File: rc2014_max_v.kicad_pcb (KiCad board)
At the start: 4 copper layers, 101.6 x 50.8 mm, 128 parts, among them J1 M3 Mounting Hole, J2 Conn_01x40, J3 Conn_01x24, J4 USB_B_Micro, J5 AVR-JTAG-10, J6 Pro Bus, J7 PMOD1, J8 PMOD, SW1 SW_Push, SW2 SW_Push, U1 TXB0108PWR, U10 FT2232H, U11 5M1270ZT144C5N, U12 93LCxxBxxOT, U13 IS61LV5128AL-10TLI, U14 Si5351A-B-GT, U15 TXB0108PWR, U16 TXB0108PWR, U18 MIC5356-SGYMME, U2 TXB0108PWR, U3 TXB0108PWR, U4 TXB0108PWR, U5 TXB0108PWR, U6 TXB0108PWR, U7 TXB0108PWR, U8 MIC5356-SGYMME, U9 TPD2EUSB30, X1 CB3LV-3I-100M0000, Y1 25MHZ 8PF

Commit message: Updated BOM
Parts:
- removed C20, C22: 100nF, Capacitor_SMD:C_0603_1608Metric_Pad1.05x0.95mm_HandSolder
- removed C21: 2.2uF, Capacitor_SMD:C_0603_1608Metric_Pad1.05x0.95mm_HandSolder
- removed U10: FT2232H, Package_QFP:LQFP-64_10x10mm_P0.5mm
- added JP2: Jumper_3_Bridged12, Connector_PinHeader_2.54mm:PinHeader_1x03_P2.54mm_Horizontal, F.Cu at (163.2, 80.8)
- JP1: footprint Connector_PinHeader_2.54mm:PinHeader_1x03_P2.54mm_Vertical -> Connector_PinHeader_2.54mm:PinHeader_1x03_P2.54mm_Horizontal
- RN8, RN9: moved to B.Cu
- U8: value MIC5356-SGYMME -> FT2232H; footprint Package_SO:MSOP-8-1EP_3x3mm_P0.65mm_EP2.5x3mm_Mask1.73x2.36mm_ThermalVias -> Package_QFP:TQFP-64_10x10mm_P0.5mm; moved to F.Cu
- moved U8 23.7 mm to (150.8, 103.3), turned to 180 degrees
- moved U16 8.59 mm to (117.6, 86.5)
- moved RN4 8.48 mm to (157.8, 110.9)
- moved C35 8.05 mm to (117.6, 83.5)
- moved D1 6.27 mm to (148.7, 111.6)
- moved R8 6.27 mm to (152.4, 111.6)
- moved R7 6.11 mm to (167.0, 83.8)
- moved C23 6.00 mm to (169.1, 85.7)
- moved RN8 5.86 mm to (164.0, 108.9)
- moved RN9 5.70 mm to (164.0, 116.3)
- moved JP1 2.65 mm to (84.0, 89.2)
- moved C34 2.55 mm to (105.0, 83.6)
- moved RN3 2.44 mm to (141.1, 79.7)
- moved J6 2.40 mm to (92.4, 80.6)
- moved U15 2.21 mm to (104.7, 86.7)
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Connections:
- C10 pad 1: +3V3 -> 3V3
- C11 pad 1: +3V3 -> 3V3
- C12 pad 1: +3V3 -> 3V3
- C13 pad 1: +3V3 -> 3V3
- C14 pad 1: +3V3 -> 3V3
- C15 pad 2: 5V -> 5V_R
- C24 pad 1: +3V3 -> 3V3
- C25 pad 1: +3V3 -> 3V3
- C26 pad 1: +3V3 -> 3V3
- C27 pad 1: +3V3 -> 3V3
- C28 pad 1: +1V8 -> 1V8
- C29 pad 1: +1V8 -> 1V8
- C30 pad 1: +1V8 -> 1V8
- C31 pad 1: +3V3 -> 3V3
- C32 pad 1: +3V3 -> 3V3
- C33 pad 1: +3V3 -> 3V3
- C38 pad 1: +3V3 -> GND
- C39 pad 1: +3V3 -> GND
- C40 pad 1: +3V3 -> GND
- C41 pad 1: +3V3 -> GND
- C8 pad 1: +3V3 -> 3V3
- C9 pad 1: +3V3 -> 3V3
- J2 pad 18: 5V -> 5V_R
- J3 pad 2: 5V -> 5V_R
- J4 pad 1: Net-(C21-Pad1) -> 5V_U
- J5 pad 4: +3V3 -> 3V3
- J5 pad 6: +3V3 -> 3V3
- J7 pad 12: +3V3 -> GND
- J7 pad 6: +3V3 -> GND
- J8 pad 12: +3V3 -> GND
- J8 pad 6: +3V3 -> GND
- JP1 pad 1: +3V3 -> 3V3
- L1 pad 1: +3V3 -> 3V3
- L2 pad 1: +3V3 -> 3V3
- R10 pad 1: +3V3 -> 3V3
- R11 pad 1: +3V3 -> 3V3
- R13 pad 1: +3V3 -> 3V3
- R14 pad 1: +3V3 -> 3V3
- R6 pad 1: +3V3 -> 3V3
- R8 pad 1: +3V3 -> 3V3
- RN1 pad 5: +3V3 -> 3V3
- RN1 pad 6: +3V3 -> 3V3
- RN1 pad 7: +3V3 -> 3V3
- RN1 pad 8: +3V3 -> 3V3
- RN3 pad 5: +3V3 -> 3V3
- RN3 pad 6: +3V3 -> 3V3
- RN3 pad 7: +3V3 -> 3V3
- RN4 pad 5: +3V3 -> 3V3
- RN4 pad 6: +3V3 -> 3V3
- RN4 pad 7: +3V3 -> 3V3
- RN4 pad 8: +3V3 -> 3V3
- RN5 pad 5: +3V3 -> GND
- RN5 pad 6: +3V3 -> GND
- RN5 pad 7: +3V3 -> GND
- RN5 pad 8: +3V3 -> GND
- RN6 pad 5: +3V3 -> 3V3
- RN6 pad 6: +3V3 -> 3V3
- RN6 pad 7: +3V3 -> 3V3
- RN6 pad 8: +3V3 -> 3V3
- RN7 pad 5: +3V3 -> 3V3
- RN7 pad 6: +3V3 -> 3V3
- RN7 pad 7: +3V3 -> 3V3
- RN7 pad 8: +3V3 -> 3V3
- U1 pad 2: +3V3 -> 3V3
- U12 pad 6: +3V3 -> 3V3
- U13 pad 11: +3V3 -> GND
- U13 pad 33: +3V3 -> GND
- U14 pad 1: +3V3 -> 3V3
- U14 pad 7: +3V3 -> 3V3
- U15 pad 2: +3V3 -> 3V3
- U16 pad 2: +3V3 -> 3V3
- U2 pad 2: +3V3 -> 3V3
- U3 pad 2: +3V3 -> 3V3
- U4 pad 2: +3V3 -> 3V3
- U5 pad 2: +3V3 -> 3V3
- U6 pad 2: +3V3 -> 3V3
- U7 pad 2: +3V3 -> 3V3
- U8 pad 1: Net-(C21-Pad1) -> GND
- U8 pad 2: GND -> CLK_12Mhz
- U8 pad 4: Net-(C21-Pad1) -> Net-(C18-Pad1)
- U8 pad 5: Net-(C21-Pad1) -> GND
- U8 pad 6: (no net) -> Net-(R5-Pad2)
- U8 pad 7: +1V8 -> Net-(J4-Pad3)
- U8 pad 8: +3V3 -> Net-(J4-Pad2)
- U8 pad 9: GND -> Net-(C16-Pad1)
- X1 pad 1: +3V3 -> 3V3
- X1 pad 4: +3V3 -> 3V3
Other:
- board text added: "PWR"
- board text removed: "JTAG PWR"

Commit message: updated descriptions and part #'s
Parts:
- D2, D3, D4, D5, D6, D7, D8, D9: value Blue -> Red
- RN10, RN11: moved to B.Cu
- U12: value 93LCxxBxxOT -> 93LC46BT-I/OT
- moved RN11 6.44 mm to (163.2, 98.9), turned to 0 degrees
- moved RN10 6.42 mm to (163.3, 89.9), turned to 0 degrees
- moved C16 3.98 mm to (159.5, 102.6)
- moved C17 3.98 mm to (159.5, 104.1)
- moved C18 3.98 mm to (159.5, 105.6)
- moved C19 3.98 mm to (159.5, 107.1)
- moved C14 2.57 mm to (162.6, 113.8)
- moved C40 2.57 mm to (168.0, 112.2)
- moved C41 2.57 mm to (168.0, 119.6)
- moved C5 2.57 mm to (162.7, 120.1)
- moved D10 2.57 mm to (166.8, 107.1)
- moved D11 2.57 mm to (166.8, 115.8)
- moved C38 2.41 mm to (168.1, 95.4)
- moved C39 2.41 mm to (168.1, 102.7)
- moved D12 2.41 mm to (166.9, 89.9)
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
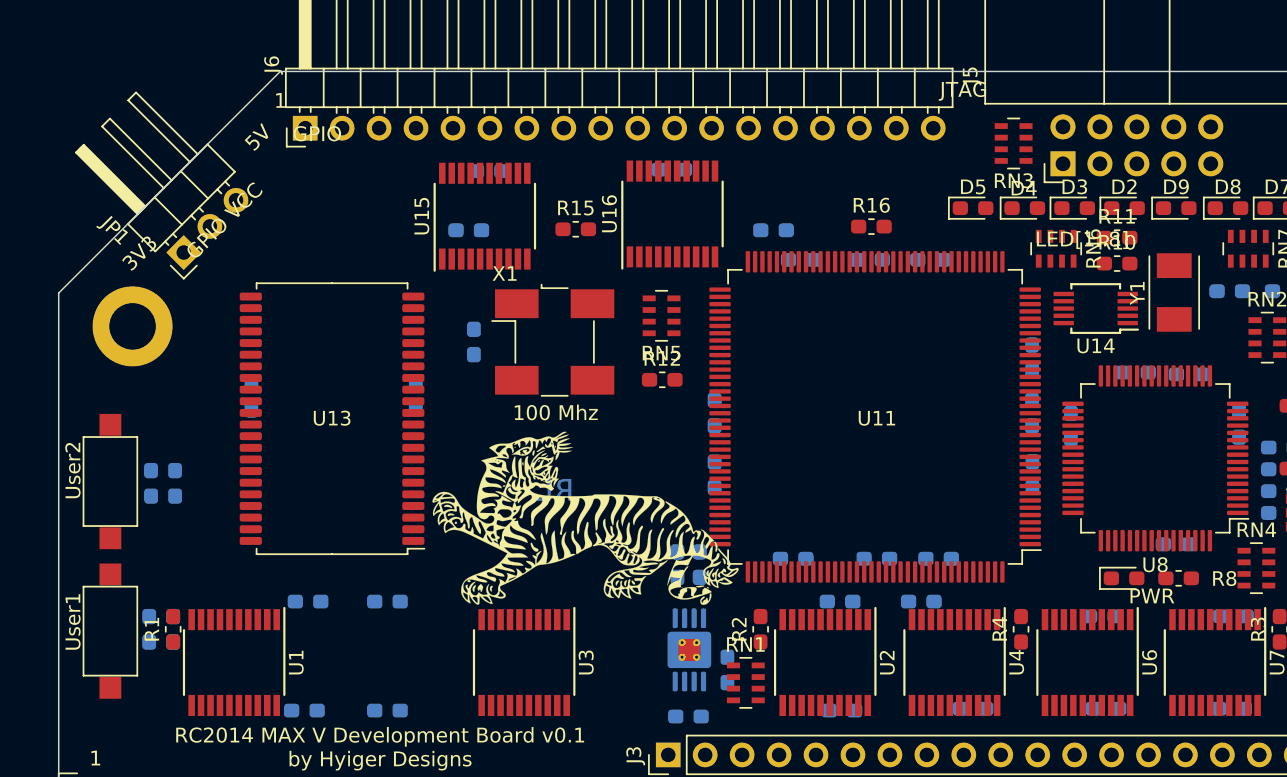
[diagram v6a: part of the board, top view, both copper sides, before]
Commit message: added clock controller/programmer
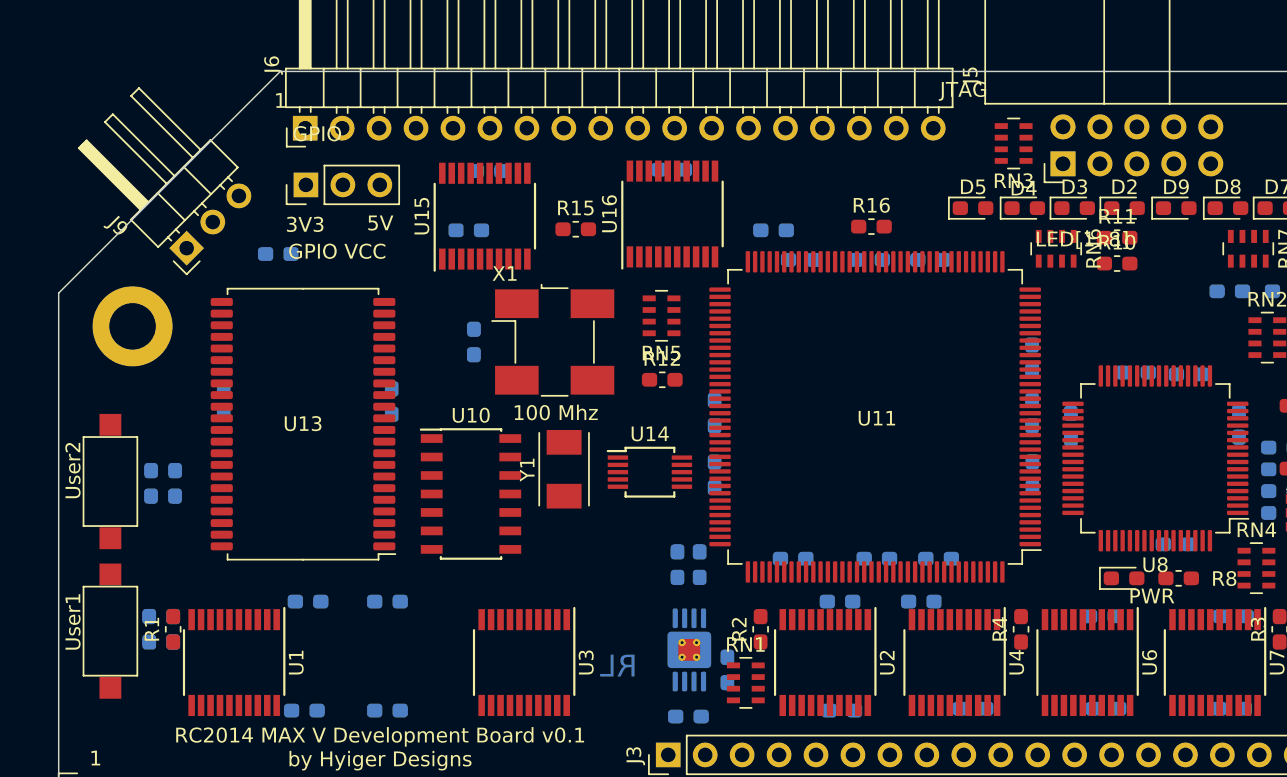
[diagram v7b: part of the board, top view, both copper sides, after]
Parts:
- removed G***: LOGO, Logos:asian_tiger
- added J9: UPDI TTL, Connector_PinHeader_2.54mm:PinHeader_1x03_P2.54mm_Horizontal, F.Cu at (84.2, 88.9)
- added R17: 4K7, Resistor_SMD:R_0603_1608Metric_Pad1.05x0.95mm_HandSolder, B.Cu at (90.5, 89.3)
- added U10: ATtiny1614-SS, Package_SO:SOIC-14_3.9x8.7mm_P1.27mm, F.Cu at (103.8, 105.8)
- JP1: footprint Connector_PinHeader_2.54mm:PinHeader_1x03_P2.54mm_Horizontal -> Connector_PinHeader_2.54mm:PinHeader_1x03_P2.54mm_Vertical
- moved Y1 43.7 mm to (110.2, 104.1)
- moved U14 32.6 mm to (116.1, 104.3), turned to 0 degrees
- moved JP1 9.60 mm to (92.4, 84.5), turned to 90 degrees
- moved U13 2.03 mm to (92.2, 101.0)
- moved C24 1.91 mm to (86.8, 99.3)
- moved C27 1.69 mm to (98.3, 99.4)

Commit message: parts placement
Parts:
- moved U12 17.2 mm to (144.7, 110.9)
- moved C2 13.0 mm to (110.9, 122.6)
- moved C9 12.7 mm to (110.7, 112.1)
- moved C10 3.95 mm to (131.3, 116.5)
- moved C3 3.35 mm to (131.3, 118.0)
- moved C1 2.64 mm to (90.8, 122.8)
- moved C8 2.11 mm to (90.8, 112.0)
- moved R8 1.11 mm to (153.5, 111.5)
- moved D1 0.28 mm to (149.0, 111.6)
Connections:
- U2 pad 12: ~M1 -> ~RFSH
- U2 pad 13: ~RFSH -> ~M1
- U2 pad 14: ~RESET -> ~PAGE
- U2 pad 15: ~PAGE -> ~RESET
- U2 pad 16: CLK -> CLK2
- U2 pad 17: CLK2 -> CLK
- U2 pad 4: CLK2_F -> CLK_F
- U2 pad 5: CLK_F -> CLK2_F
- U2 pad 6: ~PAGE_F -> ~RESET_F
- U2 pad 7: ~RESET_F -> ~PAGE_F
- U2 pad 8: ~RFSH~_F -> ~M1_F
- U2 pad 9: ~M1_F -> ~RFSH~_F
- U4 pad 12: ~MREQ -> ~HALT
- U4 pad 13: ~HALT -> ~MREQ
- U4 pad 8: ~HALT_F -> ~MREQ_F
- U4 pad 9: ~MREQ_F -> ~HALT_F
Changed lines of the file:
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@@
     (aux_axis_origin 0 0)
     (grid_origin 75.438 127.508)
-    (visible_elements FFFFF77F)
+    (visible_elements FFFFFF7F)
     (pcbplotparams
       (layerselection 0x010f0_ffffffff)
@@
       (net 31 ~WR))
     (pad 13 smd rect (at 2.95 1.625 270) (size 1.45 0.45) (layers F.Cu F.Paste F.Mask)
-      (net 40 ~HALT))
-    (pad 12 smd rect (at 2.95 2.275 270) (size 1.45 0.45) (layers F.Cu F.Paste F.Mask)
       (net 32 ~MREQ))
+    (pad 12 smd rect (at 2.95 2.275 270) (size 1.45 0.45) (layers F.Cu F.Paste F.Mask)
+      (net 40 ~HALT))
     (pad 11 smd rect (at 2.95 2.925 270) (size 1.45 0.45) (layers F.Cu F.Paste F.Mask)
       (net 2 GND))
@@
       (net 201 OE_C))
     (pad 9 smd rect (at -2.95 2.275 270) (size 1.45 0.45) (layers F.Cu F.Paste F.Mask)
-      (net 193 ~MREQ_F))
-    (pad 8 smd rect (at -2.95 1.625 270) (size 1.45 0.45) (layers F.Cu F.Paste F.Mask)
       (net 118 ~HALT_F))
+    (pad 8 smd rect (at -2.95 1.625 270) (size 1.45 0.45) (layers F.Cu F.Paste F.Mask)
+      (net 193 ~MREQ_F))
     (pad 7 smd rect (at -2.95 0.975 270) (size 1.45 0.45) (layers F.Cu F.Paste F.Mask)
       (net 194 ~WR_F))
@@
       (net 35 ~INT))
     (pad 17 smd rect (at 2.95 -0.975 270) (size 1.45 0.45) (layers F.Cu F.Paste F.Mask)
-      (net 202 CLK2))
-    (pad 16 smd rect (at 2.95 -0.325 270) (size 1.45 0.45) (layers F.Cu F.Paste F.Mask)
       (net 33 CLK))
+    (pad 16 smd rect (at 2.95 -0.325 270) (size 1.45 0.45) (layers F.Cu F.Paste F.Mask)
+      (net 202 CLK2))
     (pad 15 smd rect (at 2.95 0.325 270) (size 1.45 0.45) (layers F.Cu F.Paste F.Mask)
-      (net 28 ~PAGE))
-    (pad 14 smd rect (at 2.95 0.975 270) (size 1.45 0.45) (layers F.Cu F.Paste F.Mask)
       (net 36 ~RESET))
+    (pad 14 smd rect (at 2.95 0.975 270) (size 1.45 0.45) (layers F.Cu F.Paste F.Mask)
+      (net 28 ~PAGE))
     (pad 13 smd rect (at 2.95 1.625 270) (size 1.45 0.45) (layers F.Cu F.Paste F.Mask)
-      (net 203 ~RFSH))
-    (pad 12 smd rect (at 2.95 2.275 270) (size 1.45 0.45) (layers F.Cu F.Paste F.Mask)
       (net 34 ~M1))
+    (pad 12 smd rect (at 2.95 2.275 270) (size 1.45 0.45) (layers F.Cu F.Paste F.Mask)
+      (net 203 ~RFSH))
     (pad 11 smd rect (at 2.95 2.925 270) (size 1.45 0.45) (layers F.Cu F.Paste F.Mask)
       (net 2 GND))
@@
       (net 201 OE_C))
     (pad 9 smd rect (at -2.95 2.275 270) (size 1.45 0.45) (layers F.Cu F.Paste F.Mask)
-      (net 192 ~M1_F))
-    (pad 8 smd rect (at -2.95 1.625 270) (size 1.45 0.45) (layers F.Cu F.Paste F.Mask)
       (net 205 ~RFSH~_F))
+    (pad 8 smd rect (at -2.95 1.625 270) (size 1.45 0.45) (layers F.Cu F.Paste F.Mask)
+      (net 192 ~M1_F))
     (pad 7 smd rect (at -2.95 0.975 270) (size 1.45 0.45) (layers F.Cu F.Paste F.Mask)
-      (net 116 ~RESET_F))
-    (pad 6 smd rect (at -2.95 0.325 270) (size 1.45 0.45) (layers F.Cu F.Paste F.Mask)
       (net 102 ~PAGE_F))
+    (pad 6 smd rect (at -2.95 0.325 270) (size 1.45 0.45) (layers F.Cu F.Paste F.Mask)
+      (net 116 ~RESET_F))
     (pad 5 smd rect (at -2.95 -0.325 270) (size 1.45 0.45) (layers F.Cu F.Paste F.Mask)
-      (net 100 CLK_F))
-    (pad 4 smd rect (at -2.95 -0.975 270) (size 1.45 0.45) (layers F.Cu F.Paste F.Mask)
       (net 204 CLK2_F))
+    (pad 4 smd rect (at -2.95 -0.975 270) (size 1.45 0.45) (layers F.Cu F.Paste F.Mask)
+      (net 100 CLK_F))
     (pad 3 smd rect (at -2.95 -1.625 270) (size 1.45 0.45) (layers F.Cu F.Paste F.Mask)
       (net 117 ~INT_F))
@@
   )
   (module Capacitor_SMD:C_0603_1608Metric_Pad1.05x0.95mm_HandSolder (layer B.Cu)
-    (at 129.286 120.65)
+    (at 131.318 117.983)
     (descr "Capacitor SMD 0603 (1608 Metric), square (rectangular) end terminal, IPC_7351 nominal with elongated pad for handsoldering. (Body size source: http://www.tortai-tech.com/upload/download/2011102023233369053.pdf), generated with kicad-footprint-generator")
     (tags "capacitor handsolder")
@@
   )
   (module Capacitor_SMD:C_0603_1608Metric_Pad1.05x0.95mm_HandSolder (layer B.Cu)
-    (at 98.044 120.65)
+    (at 110.871 122.555)
     (descr "Capacitor SMD 0603 (1608 Metric), square (rectangular) end terminal, IPC_7351 nominal with elongated pad for handsoldering. (Body size source: http://www.tortai-tech.com/upload/download/2011102023233369053.pdf), generated with kicad-footprint-generator")
     (tags "capacitor handsolder")
@@
   )
   (module Capacitor_SMD:C_0603_1608Metric_Pad1.05x0.95mm_HandSolder (layer B.Cu)
-    (at 92.329 120.65)
+    (at 90.805 122.809)
     (descr "Capacitor SMD 0603 (1608 Metric), square (rectangular) end terminal, IPC_7351 nominal with elongated pad for handsoldering. (Body size source: http://www.tortai-tech.com/upload/download/2011102023233369053.pdf), generated with kicad-footprint-generator")
     (tags "capacitor handsolder")
@@
   )
   (module Capacitor_SMD:C_0603_1608Metric_Pad1.05x0.95mm_HandSolder (layer B.Cu)
-    (at 129.159 113.157)
+    (at 131.318 116.459)
     (descr "Capacitor SMD 0603 (1608 Metric), square (rectangular) end terminal, IPC_7351 nominal with elongated pad for handsoldering. (Body size source: http://www.tortai-tech.com/upload/download/2011102023233369053.pdf), generated with kicad-footprint-generator")
     (tags "capacitor handsolder")
@@
   )
   (module Capacitor_SMD:C_0603_1608Metric_Pad1.05x0.95mm_HandSolder (layer B.Cu)
-    (at 98.044 113.157)
+    (at 110.744 112.141)
     (descr "Capacitor SMD 0603 (1608 Metric), square (rectangular) end terminal, IPC_7351 nominal with elongated pad for handsoldering. (Body size source: http://www.tortai-tech.com/upload/download/2011102023233369053.pdf), generated with kicad-footprint-generator")
     (tags "capacitor handsolder")
@@
   )
   (module Capacitor_SMD:C_0603_1608Metric_Pad1.05x0.95mm_HandSolder (layer B.Cu)
-    (at 92.583 113.157)
+    (at 90.805 112.014)
     (descr "Capacitor SMD 0603 (1608 Metric), square (rectangular) end terminal, IPC_7351 nominal with elongated pad for handsoldering. (Body size source: http://www.tortai-tech.com/upload/download/2011102023233369053.pdf), generated with kicad-footprint-generator")
     (tags "capacitor handsolder")
@@
   )
   (module LED_SMD:LED_0603_1608Metric_Pad1.05x0.95mm_HandSolder (layer F.Cu)
-    (at 148.688 111.558)
+    (at 148.971 111.558)
     (descr "LED SMD 0603 (1608 Metric), square (rectangular) end terminal, IPC_7351 nominal, (Body size source: http://www.tortai-tech.com/upload/download/2011102023233369053.pdf), generated with kicad-footprint-generator")
     (tags "LED handsolder")
@@
   )
   (module Resistor_SMD:R_0603_1608Metric_Pad1.05x0.95mm_HandSolder (layer F.Cu)
-    (at 152.438 111.558 180)
+    (at 153.543 111.506 180)
     (descr "Resistor SMD 0603 (1608 Metric), square (rectangular) end terminal, IPC_7351 nominal with elongated pad for handsoldering. (Body size source: http://www.tortai-tech.com/upload/download/2011102023233369053.pdf), generated with kicad-footprint-generator")
     (tags "resistor handsolder")
@@
   )
   (module Package_TO_SOT_SMD:SOT-23-6 (layer F.Cu)
-    (at 161.438 107.058)
+    (at 144.653 110.871)
     (descr "6-pin SOT-23 package")
     (tags SOT-23-6)
